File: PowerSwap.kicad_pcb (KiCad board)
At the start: 2 copper layers, 0 parts

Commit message: Imported footprints
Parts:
- added C1: 4.7UF, Capacitors_SMD:C_0805, F.Cu at (170.7, 117.8)
- added C2: 22UF, Capacitors_SMD:C_1210, F.Cu at (176.0, 116.7)
- added C3: 0.1UF, Capacitors_SMD:C_0805, F.Cu at (183.9, 108.1)
- added L1: 2.2uH, PowerSwap:LQH3NPN2R2MM0L, F.Cu at (165.8, 119.9)
- added P1: CONN_01X02, Pin_Headers:Pin_Header_Straight_1x02, F.Cu at (152.4, 111.1)
- added P2: CONN_01X02, Pin_Headers:Pin_Header_Straight_1x02, F.Cu at (152.4, 121.9)
- added P3: TST, Measurement_Points:Measurement_Point_Square-SMD-Pad_Small, F.Cu at (158.8, 109.8)
- added P4: TST, Measurement_Points:Measurement_Point_Square-SMD-Pad_Small, F.Cu at (164.1, 109.8)
- added P5: TST, Measurement_Points:Measurement_Point_Square-SMD-Pad_Small, F.Cu at (169.4, 109.8)
- added P6: TST, Measurement_Points:Measurement_Point_Square-SMD-Pad_Small, F.Cu at (158.8, 119.6)
- added R1: 1.2M, Resistors_SMD:R_0805, F.Cu at (175.1, 123.6)
- added R2: 215K, Resistors_SMD:R_0805, F.Cu at (183.7, 114.4)
- added R3: 0, Resistors_SMD:R_0805, F.Cu at (170.1, 124.1)
- added R4: 0, Resistors_SMD:R_0805, F.Cu at (180.3, 120.7)
- added R5: 0, Resistors_SMD:R_0805, F.Cu at (184.0, 120.7)
- added U1: TPS63030, PowerSwap:TPS63030, F.Cu at (177.4, 109.0)
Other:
- rule pad_to_mask_clearance: 0 -> 0.0762

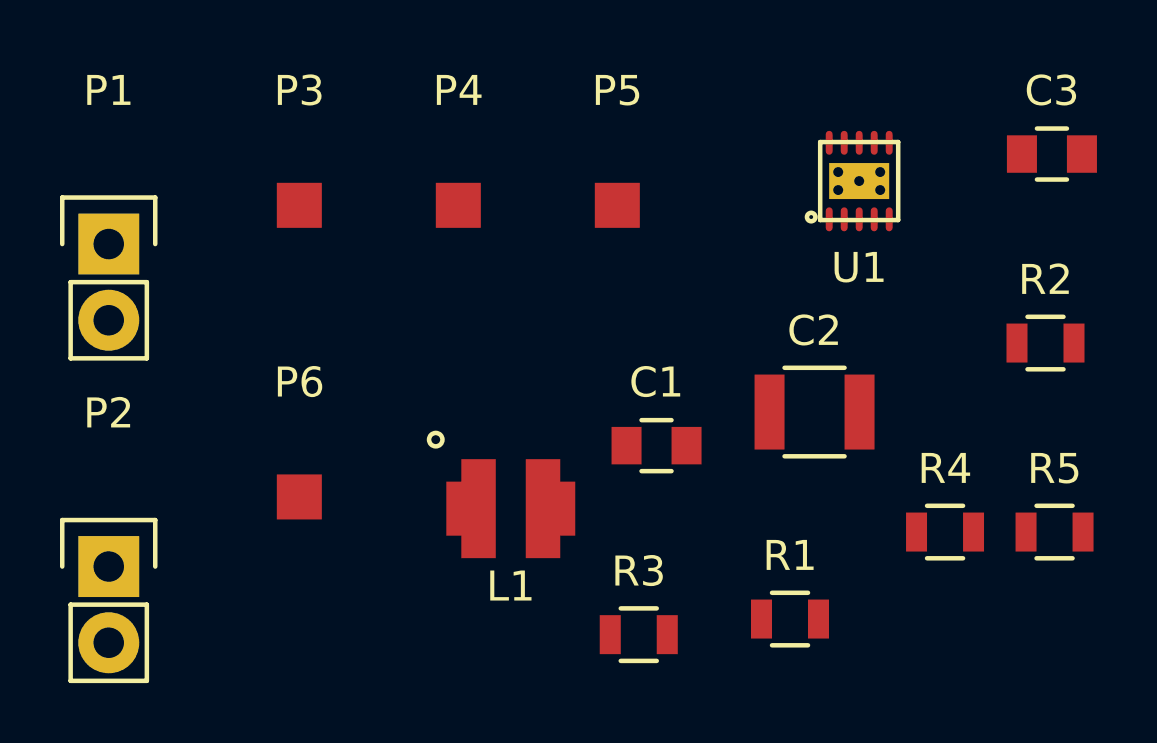
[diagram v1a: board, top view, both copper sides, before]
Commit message: Finished Power Swap Layout
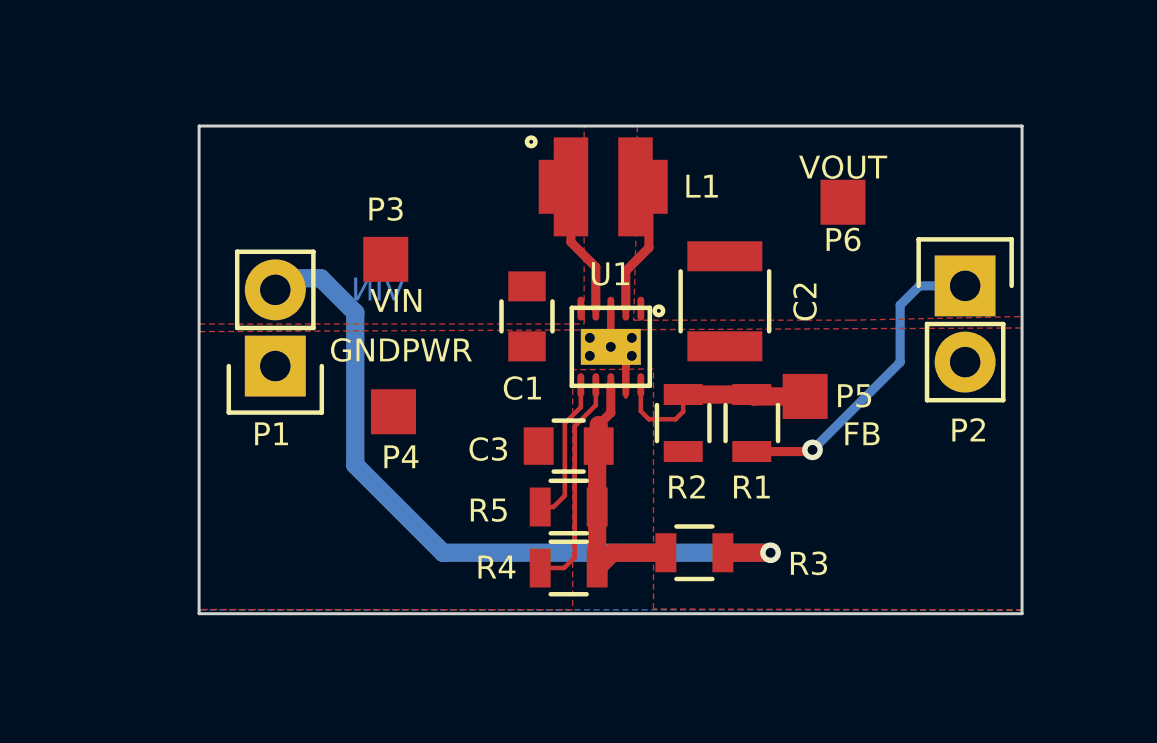
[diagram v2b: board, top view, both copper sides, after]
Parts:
- moved P2 30.0 mm to (181.0, 112.5)
- moved P6 20.6 mm to (176.9, 109.7)
- moved C3 18.8 mm to (167.8, 117.9), turned to 180 degrees
- moved R5 16.2 mm to (167.8, 119.9)
- moved R4 12.6 mm to (167.8, 121.9)
- moved R2 12.4 mm to (171.6, 117.1), turned to 270 degrees
- moved L1 11.2 mm to (168.9, 109.2)
- moved U1 9.95 mm to (169.2, 114.6), turned to 180 degrees
- moved P5 8.93 mm to (175.6, 116.2)
- moved P4 7.21 mm to (161.9, 116.7)
- moved P1 6.88 mm to (158.0, 115.2), turned to 180 degrees
- moved R1 6.66 mm to (173.9, 117.1), turned to 90 degrees
- moved C1 6.10 mm to (166.4, 113.5), turned to 270 degrees
- moved C2 4.75 mm to (173.0, 113.0), turned to 270 degrees
- moved P3 3.40 mm to (161.7, 111.6)
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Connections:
- U1 pad 11: Net-(U1-Pad11) -> GNDPWR
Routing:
- net /VIN: track 0.00 -> 24.3 mm, vias 0 -> 1
- net /VOUT: track 0.00 -> 10.5 mm, vias 0 -> 1
- net /VINA: track 0.00 -> 8.79 mm
- net Net-(R4-Pad1): track 0.00 -> 7.33 mm
- net /FB: track 0.00 -> 7.16 mm
- net Net-(L1-Pad2): track 0.00 -> 5.39 mm
- net Net-(L1-Pad1): track 0.00 -> 5.23 mm
- net Net-(R5-Pad1): track 0.00 -> 4.88 mm
- net GNDPWR: track 0.00 -> 2.30 mm
- added copper zone on F.Cu, net /VIN
- added copper zone on F.Cu, net /VOUT
- added copper zone on B.Cu, net GNDPWR
- added copper zone on F.Cu, net GNDPWR
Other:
- board outline added: 27.4 x 16.3 mm
- net class Default: clearance 0.2 -> 0.1524; trace_width 0.25 -> 0.1524; via_dia 0.6 -> 0.6858; via_drill 0.4 -> 0.3302
- rule trace_clearance: 0.2 -> 0.1524
- rule trace_min: 0.2 -> 0.1524
- rule via_min_drill: 0.3 -> 0.3302
- rule via_min_size: 0.4 -> 0.6858
- board text added: "FB"
- board text added: "GNDPWR"
- board text added: "VIN"
- board text added: "VOUT"

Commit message: Added via stitching and generated gerbers for fabrication
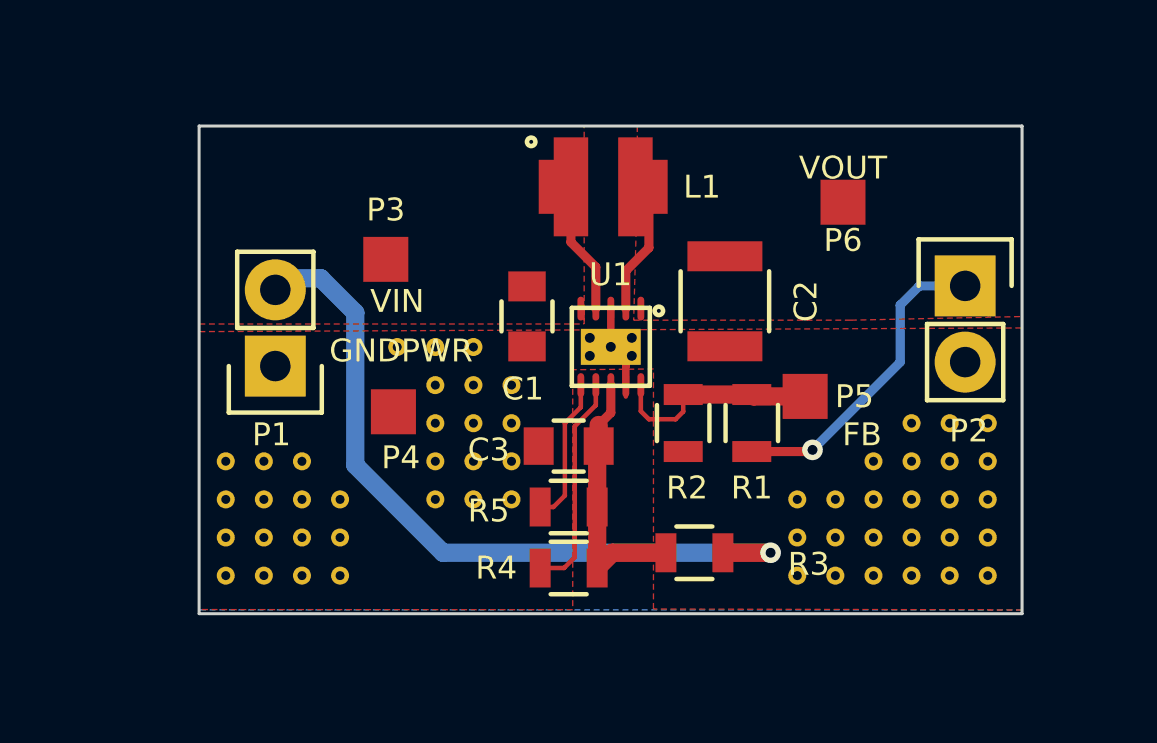
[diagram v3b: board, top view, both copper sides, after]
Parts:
- added G***: LOGO, PowerSwap:PS_Logo, F.Cu at (167.8, 106.9)
- added REF**1111: VIA-0.6mm, PowerSwap:VIA-0.6mm, F.Cu at (175.4, 119.6)
- added REF**111111: VIA-0.6mm, PowerSwap:VIA-0.6mm, F.Cu at (164.6, 114.6)
- added REF**111111: VIA-0.6mm, PowerSwap:VIA-0.6mm, F.Cu at (163.3, 114.6)
- added REF**111111: VIA-0.6mm, PowerSwap:VIA-0.6mm, F.Cu at (162.0, 114.6)
- added REF**111111: VIA-0.6mm, PowerSwap:VIA-0.6mm, F.Cu at (158.9, 118.4)
- added REF**111111: VIA-0.6mm, PowerSwap:VIA-0.6mm, F.Cu at (157.6, 118.4)
- added REF**111111: VIA-0.6mm, PowerSwap:VIA-0.6mm, F.Cu at (156.3, 118.4)
- added REF**111111: VIA-0.6mm, PowerSwap:VIA-0.6mm, F.Cu at (156.3, 119.6)
- added REF**11111111: VIA-0.6mm, PowerSwap:VIA-0.6mm, F.Cu at (163.3, 115.8)
- added REF**11111112: VIA-0.6mm, PowerSwap:VIA-0.6mm, F.Cu at (163.3, 117.1)
- added REF**11111113: VIA-0.6mm, PowerSwap:VIA-0.6mm, F.Cu at (163.3, 118.4)
- added REF**11111114: VIA-0.6mm, PowerSwap:VIA-0.6mm, F.Cu at (163.3, 119.6)
- added REF**11111121: VIA-0.6mm, PowerSwap:VIA-0.6mm, F.Cu at (164.6, 115.8)
- added REF**11111122: VIA-0.6mm, PowerSwap:VIA-0.6mm, F.Cu at (164.6, 117.1)
- added REF**11111123: VIA-0.6mm, PowerSwap:VIA-0.6mm, F.Cu at (164.6, 118.4)
- added REF**11111124: VIA-0.6mm, PowerSwap:VIA-0.6mm, F.Cu at (164.6, 119.6)
- added REF**11111131: VIA-0.6mm, PowerSwap:VIA-0.6mm, F.Cu at (165.9, 115.8)
- added REF**11111132: VIA-0.6mm, PowerSwap:VIA-0.6mm, F.Cu at (165.9, 117.1)
- added REF**11111133: VIA-0.6mm, PowerSwap:VIA-0.6mm, F.Cu at (165.9, 118.4)
- added REF**11111134: VIA-0.6mm, PowerSwap:VIA-0.6mm, F.Cu at (165.9, 119.6)
- added REF**111112: VIA-0.6mm, PowerSwap:VIA-0.6mm, F.Cu at (156.3, 120.9)
- added REF**111113: VIA-0.6mm, PowerSwap:VIA-0.6mm, F.Cu at (156.3, 122.2)
- added REF**111121: VIA-0.6mm, PowerSwap:VIA-0.6mm, F.Cu at (157.6, 119.6)
- added REF**111122: VIA-0.6mm, PowerSwap:VIA-0.6mm, F.Cu at (157.6, 120.9)
- added REF**111123: VIA-0.6mm, PowerSwap:VIA-0.6mm, F.Cu at (157.6, 122.2)
- added REF**111131: VIA-0.6mm, PowerSwap:VIA-0.6mm, F.Cu at (158.9, 119.6)
- added REF**111132: VIA-0.6mm, PowerSwap:VIA-0.6mm, F.Cu at (158.9, 120.9)
- added REF**111133: VIA-0.6mm, PowerSwap:VIA-0.6mm, F.Cu at (158.9, 122.2)
- added REF**111141: VIA-0.6mm, PowerSwap:VIA-0.6mm, F.Cu at (160.1, 119.6)
- added REF**111142: VIA-0.6mm, PowerSwap:VIA-0.6mm, F.Cu at (160.1, 120.9)
- added REF**111143: VIA-0.6mm, PowerSwap:VIA-0.6mm, F.Cu at (160.1, 122.2)
- added REF**1112: VIA-0.6mm, PowerSwap:VIA-0.6mm, F.Cu at (175.4, 120.9)
- added REF**1113: VIA-0.6mm, PowerSwap:VIA-0.6mm, F.Cu at (175.4, 122.2)
- added REF**1121: VIA-0.6mm, PowerSwap:VIA-0.6mm, F.Cu at (176.6, 119.6)
- added REF**1122: VIA-0.6mm, PowerSwap:VIA-0.6mm, F.Cu at (176.6, 120.9)
- added REF**1123: VIA-0.6mm, PowerSwap:VIA-0.6mm, F.Cu at (176.6, 122.2)
- added REF**1131: VIA-0.6mm, PowerSwap:VIA-0.6mm, F.Cu at (179.2, 117.1)
- added REF**1131: VIA-0.6mm, PowerSwap:VIA-0.6mm, F.Cu at (180.5, 117.1)
- added REF**1131: VIA-0.6mm, PowerSwap:VIA-0.6mm, F.Cu at (181.7, 117.1)
- added REF**1131: VIA-0.6mm, PowerSwap:VIA-0.6mm, F.Cu at (181.7, 118.4)
- added REF**1131: VIA-0.6mm, PowerSwap:VIA-0.6mm, F.Cu at (180.5, 118.4)
- added REF**1131: VIA-0.6mm, PowerSwap:VIA-0.6mm, F.Cu at (179.2, 118.4)
- added REF**1131: VIA-0.6mm, PowerSwap:VIA-0.6mm, F.Cu at (177.9, 118.4)
- added REF**1131: VIA-0.6mm, PowerSwap:VIA-0.6mm, F.Cu at (177.9, 119.6)
- added REF**1132: VIA-0.6mm, PowerSwap:VIA-0.6mm, F.Cu at (177.9, 120.9)
- added REF**1133: VIA-0.6mm, PowerSwap:VIA-0.6mm, F.Cu at (177.9, 122.2)
- added REF**1141: VIA-0.6mm, PowerSwap:VIA-0.6mm, F.Cu at (179.2, 119.6)
- added REF**1142: VIA-0.6mm, PowerSwap:VIA-0.6mm, F.Cu at (179.2, 120.9)
- added REF**1143: VIA-0.6mm, PowerSwap:VIA-0.6mm, F.Cu at (179.2, 122.2)
- added REF**1151: VIA-0.6mm, PowerSwap:VIA-0.6mm, F.Cu at (180.5, 119.6)
- added REF**1152: VIA-0.6mm, PowerSwap:VIA-0.6mm, F.Cu at (180.5, 120.9)
- added REF**1153: VIA-0.6mm, PowerSwap:VIA-0.6mm, F.Cu at (180.5, 122.2)
- added REF**1161: VIA-0.6mm, PowerSwap:VIA-0.6mm, F.Cu at (181.7, 119.6)
- added REF**1162: VIA-0.6mm, PowerSwap:VIA-0.6mm, F.Cu at (181.7, 120.9)
- added REF**1163: VIA-0.6mm, PowerSwap:VIA-0.6mm, F.Cu at (181.7, 122.2)
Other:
- rule pad_to_mask_clearance: 0.0762 -> 0
- board text added: "PowerSwap TPS63030 Rev 1"
